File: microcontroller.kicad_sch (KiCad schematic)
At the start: 64 parts, among them J4 Conn_01x03_Pin, J5 Conn_01x05_Pin, J6 Conn_02x04_Odd_Even, J7 Conn_02x15_Counter_Clockwise, SW2 SW_Push, SW3 SW_Push, U3 RP2040, U5 W25Q16JVSS, U6 W25Q16JVSS, Y1 12MHz/10pF, Y2 12MHz/10pF

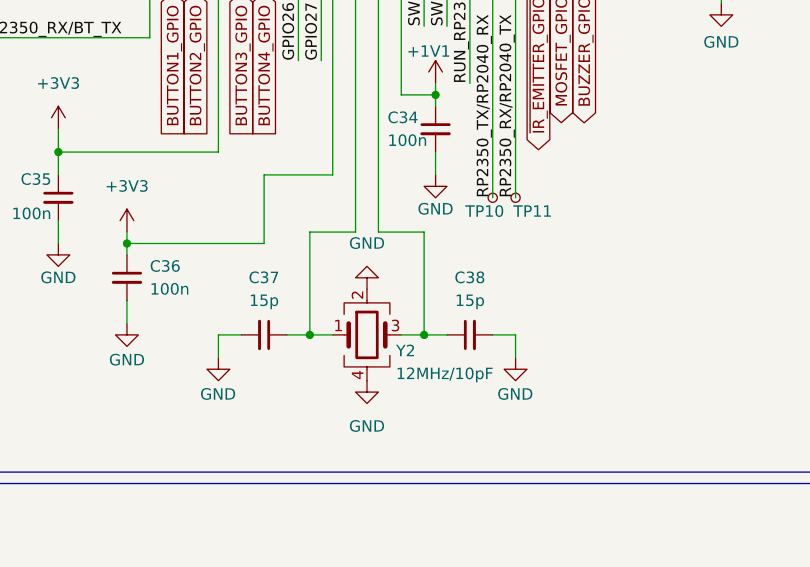
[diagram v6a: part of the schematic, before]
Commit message: wip: places rp circuitry
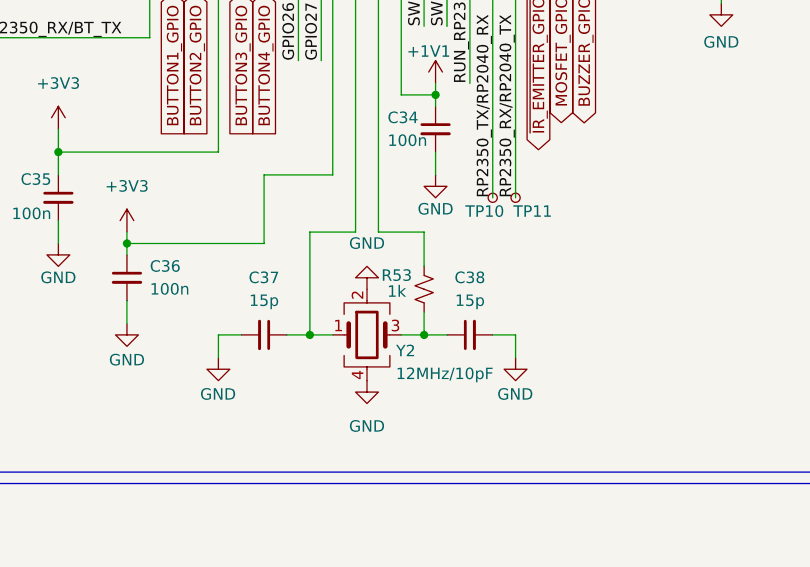
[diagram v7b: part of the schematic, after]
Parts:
- added R53: 1k, Resistor_SMD:R_0402_1005Metric, symbol Device:R_Small_US
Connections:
- net at C38.1, Y2.3: now also R53.1; no longer U4.31 (XOUT)
- new net: R53.2, U4.31 (XOUT)
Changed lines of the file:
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@@
 	)
 	(junction
-		(at 300.99 55.88)
+		(at 97.79 187.96)
 		(diameter 0)
 		(color 0 0 0 0)
 	)
 	(junction
-		(at 285.75 45.72)
+		(at 300.99 55.88)
 		(diameter 0)
 		(color 0 0 0 0)
 	)
 	(junction
-		(at 97.79 187.96)
+		(at 285.75 45.72)
 		(diameter 0)
 		(color 0 0 0 0)
@@
 	(wire
 		(pts
+			(xy 97.79 176.53) (xy 97.79 180.34)
+		)
+		(stroke
+			(width 0)
+			(type default)
+		)
+	)
+	(wire
+		(pts
 			(xy 125.73 102.87) (xy 123.19 102.87)
 		)
@@
 	(wire
 		(pts
+			(xy 97.79 185.42) (xy 97.79 187.96)
+		)
+		(stroke
+			(width 0)
+			(type default)
+		)
+	)
+	(wire
+		(pts
 			(xy 57.15 106.68) (xy 59.69 106.68)
 		)
@@
 	(wire
 		(pts
-			(xy 97.79 187.96) (xy 100.33 187.96)
-		)
-		(stroke
-			(width 0)
-			(type default)
-		)
-	)
-	(wire
-		(pts
 			(xy 191.77 124.46) (xy 194.31 124.46)
 		)
@@
 	(wire
 		(pts
+			(xy 97.79 187.96) (xy 100.33 187.96)
+		)
+		(stroke
+			(width 0)
+			(type default)
+		)
+	)
+	(wire
+		(pts
 			(xy 167.64 107.95) (xy 167.64 110.49)
 		)
@@
 	(wire
 		(pts
-			(xy 97.79 187.96) (xy 97.79 176.53)
-		)
-		(stroke
-			(width 0)
-			(type default)
-		)
-	)
-	(wire
-		(pts
 			(xy 373.38 139.7) (xy 384.81 139.7)
 		)
@@
 					(unit 1)
 				)
+			)
+		)
+	)
+	(symbol
+		(lib_id "Device:R_Small_US")
+		(at 97.79 182.88 180)
+		(unit 1)
+		(exclude_from_sim no)
+		(in_bom yes)
+		(on_board yes)
+		(dnp no)
+		(property "Reference" "R53"
+			(at 94.742 181.356 0)
+			(effects
+				(font
+					(size 1.27 1.27)
+				)
+			)
+		)
+		(property "Value" "1k"
+			(at 94.742 183.134 0)
+			(effects
+				(font
+					(size 1.27 1.27)
+				)
+			)
+		)
+		(property "Footprint" "Resistor_SMD:R_0402_1005Metric"
+			(at 97.79 182.88 0)
+			(effects
+				(font
+					(size 1.27 1.27)
+				)
+				(hide yes)
+			)
+		)
+		(property "Datasheet" "https://www.digikey.com.br/en/products/detail/yageo/RC0402JR-071KL/726408"
+			(at 97.79 182.88 0)
+			(effects
+				(font
+					(size 1.27 1.27)
+				)
+				(hide yes)
+			)
+		)
+		(property "Description" "Resistor, small US symbol"
+			(at 97.79 182.88 0)
+			(effects
+				(font
+					(size 1.27 1.27)
+				)
+				(hide yes)
+			)
+		)
+		(property "MPN" "RC0402JR-071KL"
+			(at 97.79 182.88 90)
+			(effects
+				(font
+					(size 1.27 1.27)
+				)
+				(hide yes)
+			)
+		)
+		(pin "1"
+		)
+		(pin "2"
+		)
+		(instances
+			(project "zbook"
+				(path "/b90666d0-8852-4bb1-832d-f9d855027372/d36fc6ee-483e-4a4a-988a-06a4ba308aa7"
+					(reference "R53")
+					(unit 1)
+				)

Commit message: fix: changes external header to socket
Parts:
- J7: footprint Connector_PinHeader_2.54mm:PinHeader_2x15_P2.54mm_Vertical -> Connector_PinSocket_2.54mm:PinSocket_2x15_P2.54mm_Vertical
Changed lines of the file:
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@@
 			)
 		)
-		(property "Footprint" "Connector_PinHeader_2.54mm:PinHeader_2x15_P2.54mm_Vertical"
+		(property "Footprint" "Connector_PinSocket_2.54mm:PinSocket_2x15_P2.54mm_Vertical"
 			(at 199.39 194.31 0)
 			(effects
